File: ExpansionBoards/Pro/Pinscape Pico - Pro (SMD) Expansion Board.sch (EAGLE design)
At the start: 211 parts, among them IC1 UCC27523D, IC10 UCC27523D, IC11 UCC27523D, IC12 UCC27523D, IC13 UCC27523D, IC14 UCC27523D, IC15 TLC59116FIRHBR, IC16 TLC59116FIRHBR, IC17 TLC59116FIRHBR, IC18 TLC59116FIRHBR, IC19 ULN2803ADWR, IC2 UCC27523D, IC20 ULN2803ADWR, IC21 ULN2803ADWR, IC22 ULN2803ADWR, IC23 ULN2803ADWR, IC24 SN74HC165PWR, IC25 SN74HC165PWR, IC26 SN74HC165PWR, IC27 SN74HC165PWR, IC28 LIS3DHTR, IC29 SN74LVC1G175DCKR, IC3 UCC27523D, IC30 APX809S-29SA-7, IC31 LTV-827S, IC32 ADS1115IDGSR, IC33 TLV75733PDBVR, IC34 RV-3032-C7, IC4 UCC27523D, IC5 UCC27523D, IC6 UCC27523D, IC7 UCC27523D, IC8 UCC27523D, IC9 UCC27523D, J1 640445-6, J10 1-640456-0, J11 1-640456-0, J12 1-640456-0, J13 640445-5, J14 640445-9, J15 640445-9, J16 640445-9, J18 BM03B-SRSS-TB(LF)(SN), J2 30316-6002HB, J3 1-640456-0, J4 640456-9, J5 640456-9, J6 640454-2, J7 215079-4, J8 30308-6002HB, J9 1-640456-0, Q1 BUK7K89-100EX, Q10 BUK7K89-100EX, Q11 BUK7K89-100EX, Q12 BUK7K89-100EX, Q13 BUK7K89-100EX, Q14 BUK7K89-100EX, Q15 UMA5NTR, Q16 UMA5NTR, Q17 UMA5NTR, Q18 UMA5NTR, Q19 UMA5NTR, Q2 BUK7K89-100EX, Q20 UMA5NTR, Q21 UMA5NTR, Q22 UMA5NTR, Q23 UMA5NTR, Q24 UMA5NTR, Q25 UMA5NTR, Q26 UMA5NTR, Q29 DMG2302UK-7, Q3 BUK7K89-100EX, Q4 BUK7K89-100EX, Q5 BUK7K89-100EX, Q6 BUK7K89-100EX, Q7 BUK7K89-100EX, Q8 BUK7K89-100EX, Q9 BUK7K89-100EX, SW1 TS-1187A-B-A-B, U1 BAT-HLD-001-THM

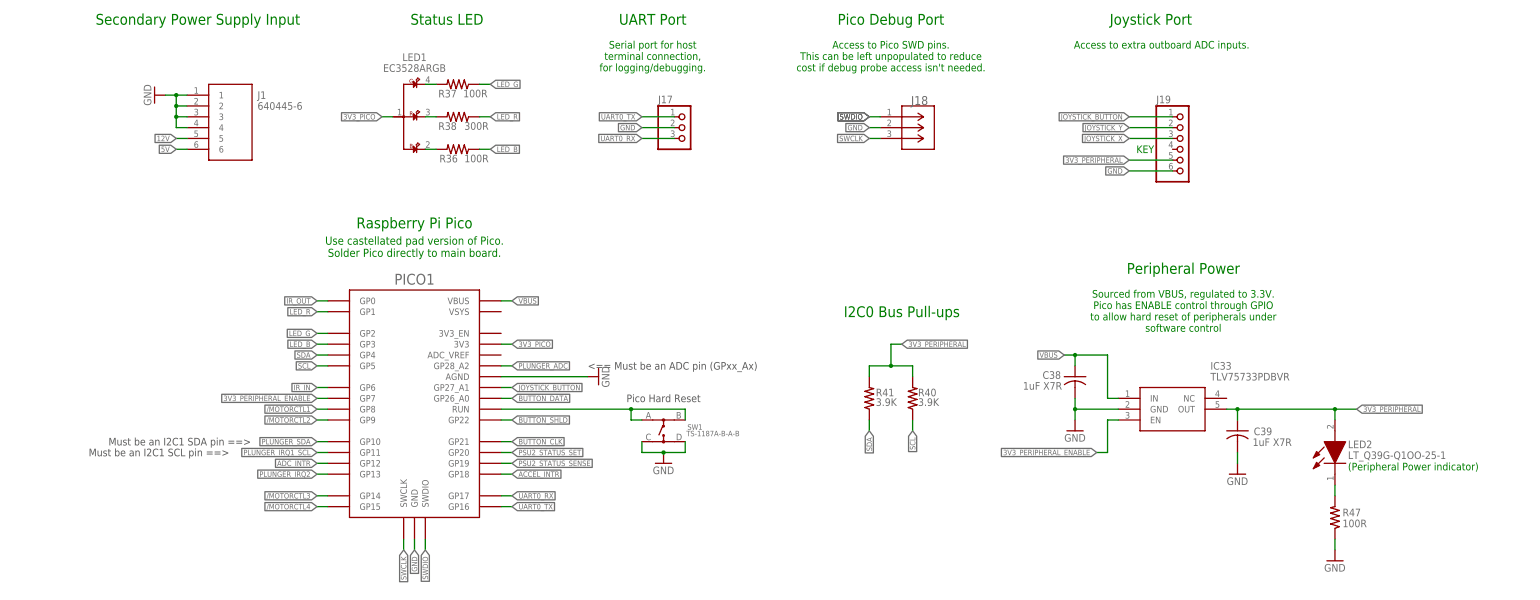
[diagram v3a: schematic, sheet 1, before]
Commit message: change to socketed Pico for Pro board
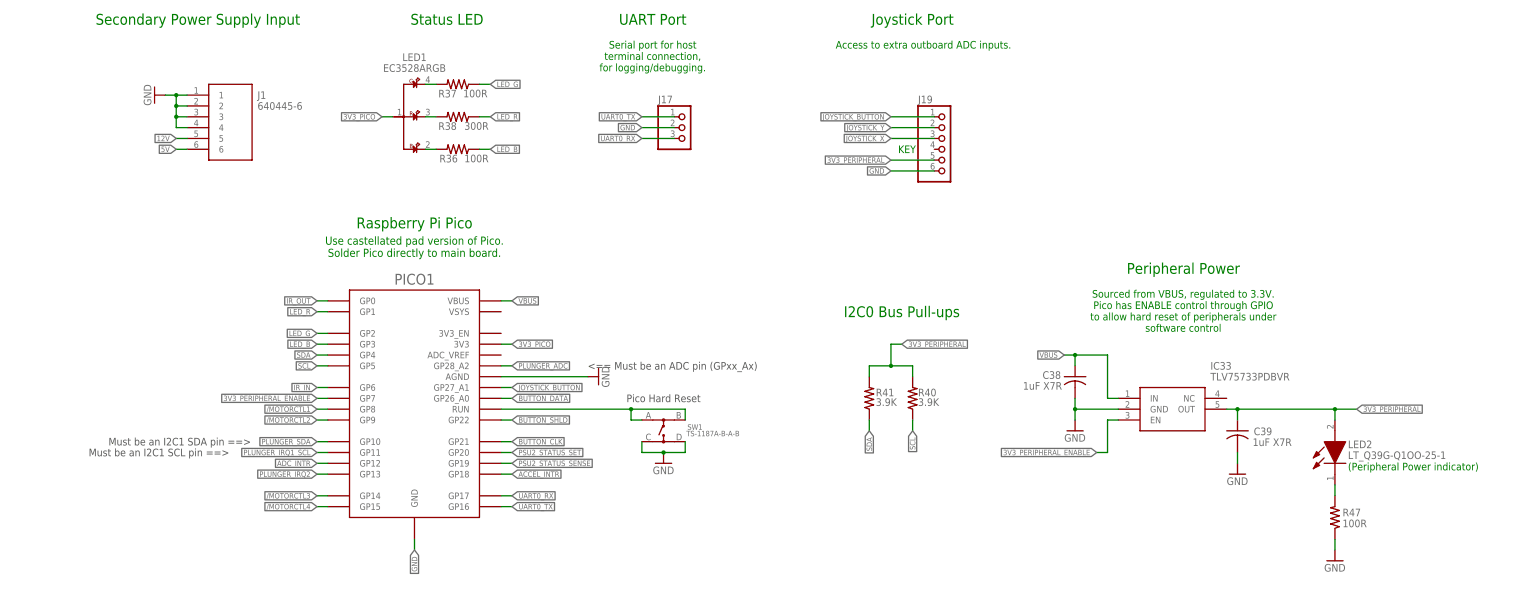
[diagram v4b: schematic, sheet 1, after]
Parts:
- removed J18: BM03B-SRSS-TB(LF)(SN), SamacSys_Parts:BM03B-SRSS-TB(LF)(SN)
- PICO1: device RaspberryPi_Pico:RPI_PICO-SMD -> RaspberryPi_Pico:RPI_PICO_NO_DEBUG
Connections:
- removed net SWCLK: J18.3, PICO1.SWCLK
- removed net SWDIO: J18.1, PICO1.SWDIO
- net GND: no longer J18.2
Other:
- note removed: "Access to Pico SWD pins. This can be left unpopulated to reduce cost if debug probe access isn't needed."
- note removed: "Pico Debug Port"
- moved on the sheet: J19

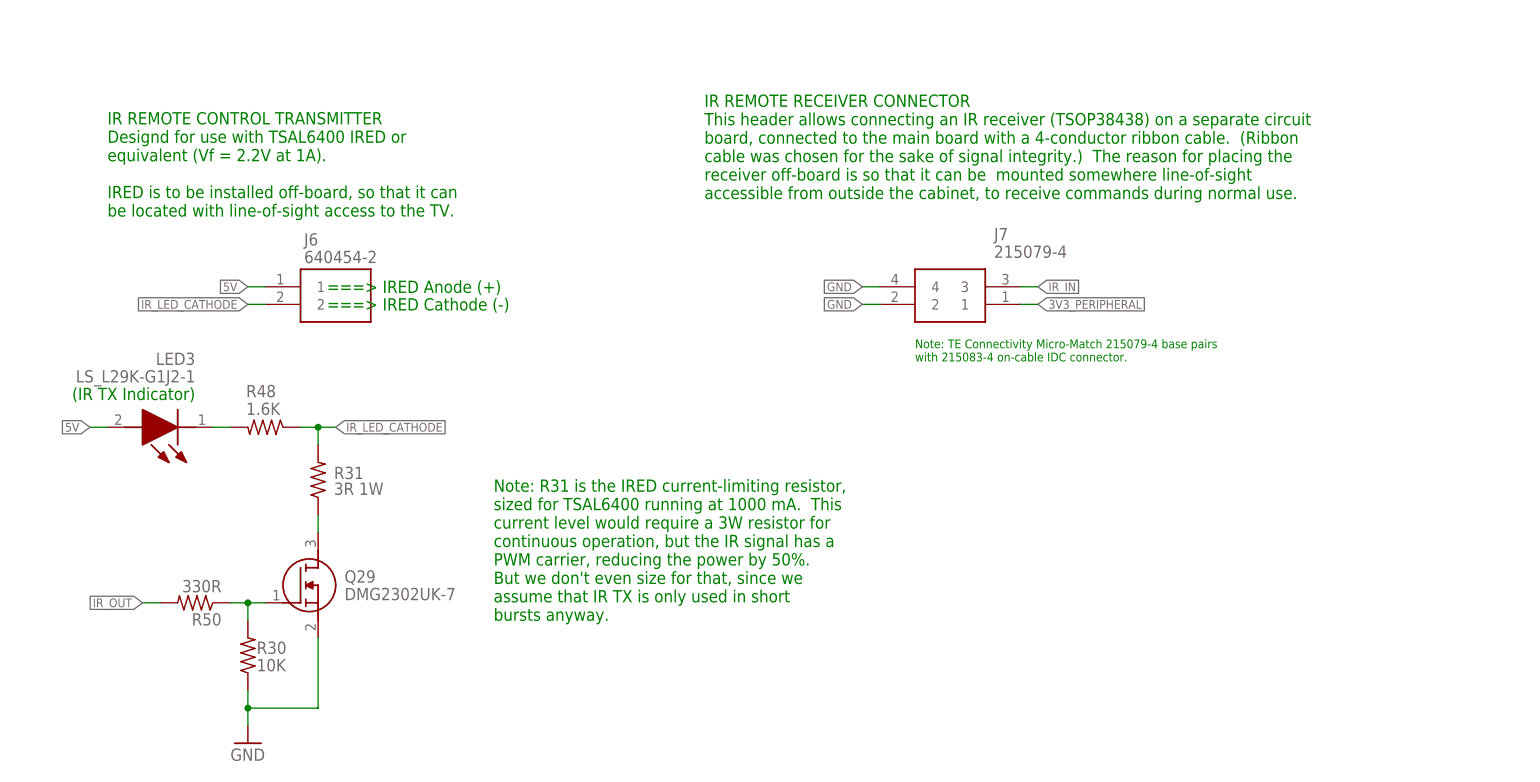
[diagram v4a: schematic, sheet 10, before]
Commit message: add tlc59116 wiring diagram to json doc; change Pro board IRED to constant-current circuit
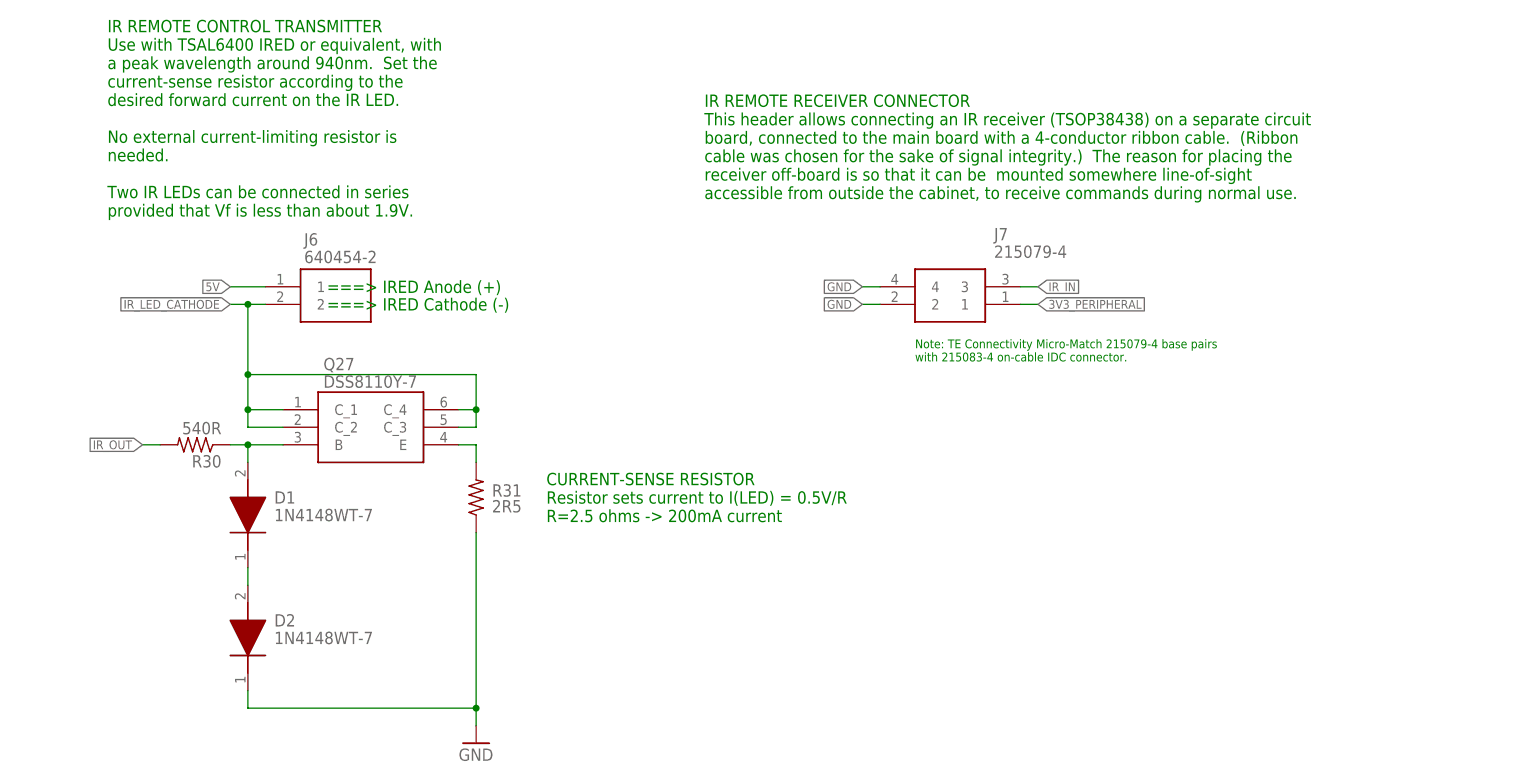
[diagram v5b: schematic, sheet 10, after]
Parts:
- removed LED3: LS_L29K-G1J2-1, SamacSys_Parts:LS_L29K-G1J2-1
- removed Q29: DMG2302UK-7, SamacSys_Parts:DMG2302UK-7
- removed R48: 1.6K, resistor:R-US_R0402
- removed R50: 330R, resistor:R-US_R0402
- added D1, D2: 1N4148WT-7, SamacSys_Parts:1N4148WT-7
- added Q27: DSS8110Y-7, SamacSys_Parts:DSS8110Y-7
- R30: value 10K -> 540R
- R31: value 3R 1W -> 2R5; device rcl:R-US_R2512 -> rcl:R-US_R0603
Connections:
- removed net N$75: LED3.K, R48.2
- new net N$81: D1.K, D2.A
- net 5V: no longer LED3.A
- net GND: now also D2.K, R31.1; no longer Q29.S, R30.1
- net IR_LED_CATHODE: now also Q27.C_1, Q27.C_2, Q27.C_3, Q27.C_4; no longer R31.2, R48.1
- net IR_OUT: now also R30.2; no longer R50.2
- net N$32: now also Q27.E, R31.2; no longer Q29.D, R31.1
- net N$77: now also D1.A, Q27.B, R30.1; no longer Q29.G, R30.2, R50.1
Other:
- note added: "CURRENT-SENSE RESISTOR Resistor sets current to I(LED) = 0.5V/R R=2.5 ohms -> 200mA current"
- note added: "IR REMOTE CONTROL TRANSMITTER Use with TSAL6400 IRED or equivalent, with a peak wavelength around 940nm. Set the current-sense resistor according to the desired forward current on the IR LED. No external current-limiting resistor is needed. Two IR LEDs can be connected in series provided that Vf is less than about 1.9V."
- note removed: "(IR TX Indicator)"
- note removed: "IR REMOTE CONTROL TRANSMITTER Designd for use with TSAL6400 IRED or equivalent (Vf = 2.2V at 1A). IRED is to be installed off-board, so that it can be located with line-of-sight access to the TV."
- note removed: "Note: R31 is the IRED current-limiting resistor, sized for TSAL6400 running at 1000 mA. This current level would require a 3W resistor for continuous operation, but the IR signal has a PWM carrier, reducing the power by 50%. But we don't even size for that, since we assume that IR TX is only used in short bursts anyway."
- moved on the sheet: R30, R31

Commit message: Update Pro and KL25Z adapter boards to make LIS3DH footprint compatible with LIS3DSH
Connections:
- net GND: now also IC28.ADC1, IC28.ADC2, IC28.ADC3
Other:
- note added: "Accelerometer - LIS3DH I2C Address 0x18 (001 1000)"
- note added: "Also pin-compatible with LIS3DSH (address 0x1E, 001 1110)"
- note removed: "Accelerometer"
- moved on the sheet: C35, IC28

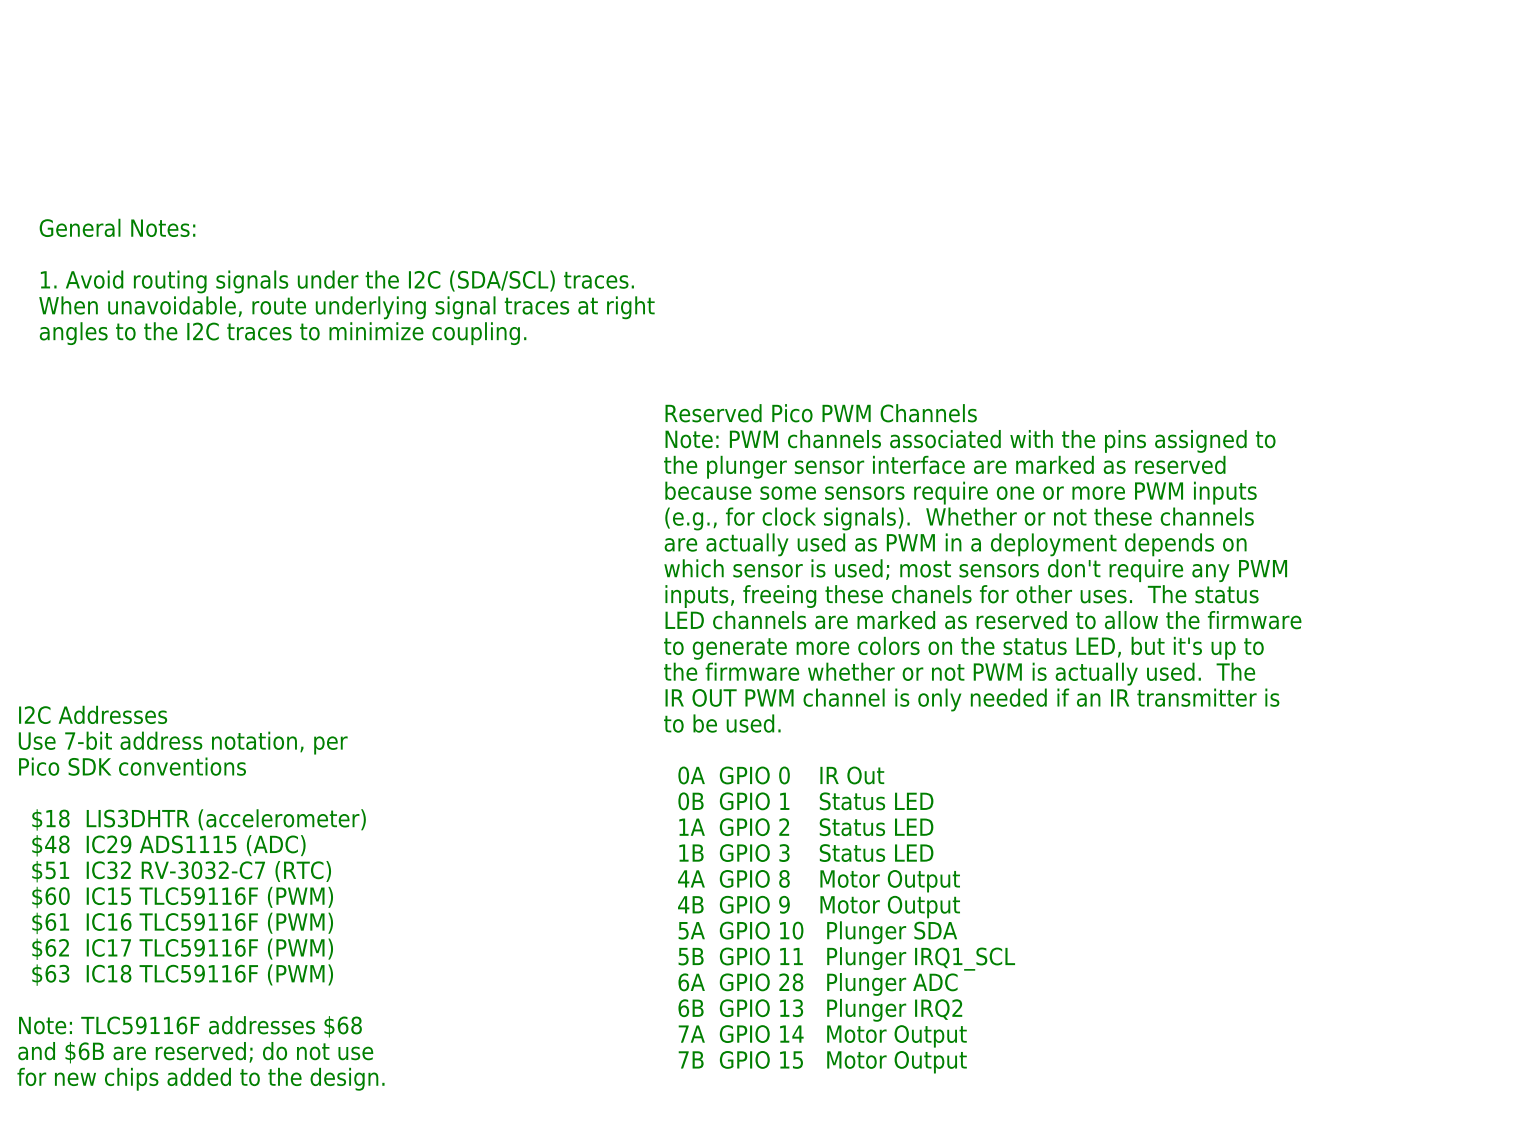
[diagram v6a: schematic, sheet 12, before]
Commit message: PCB parts lists (BOMs); power distro board edits
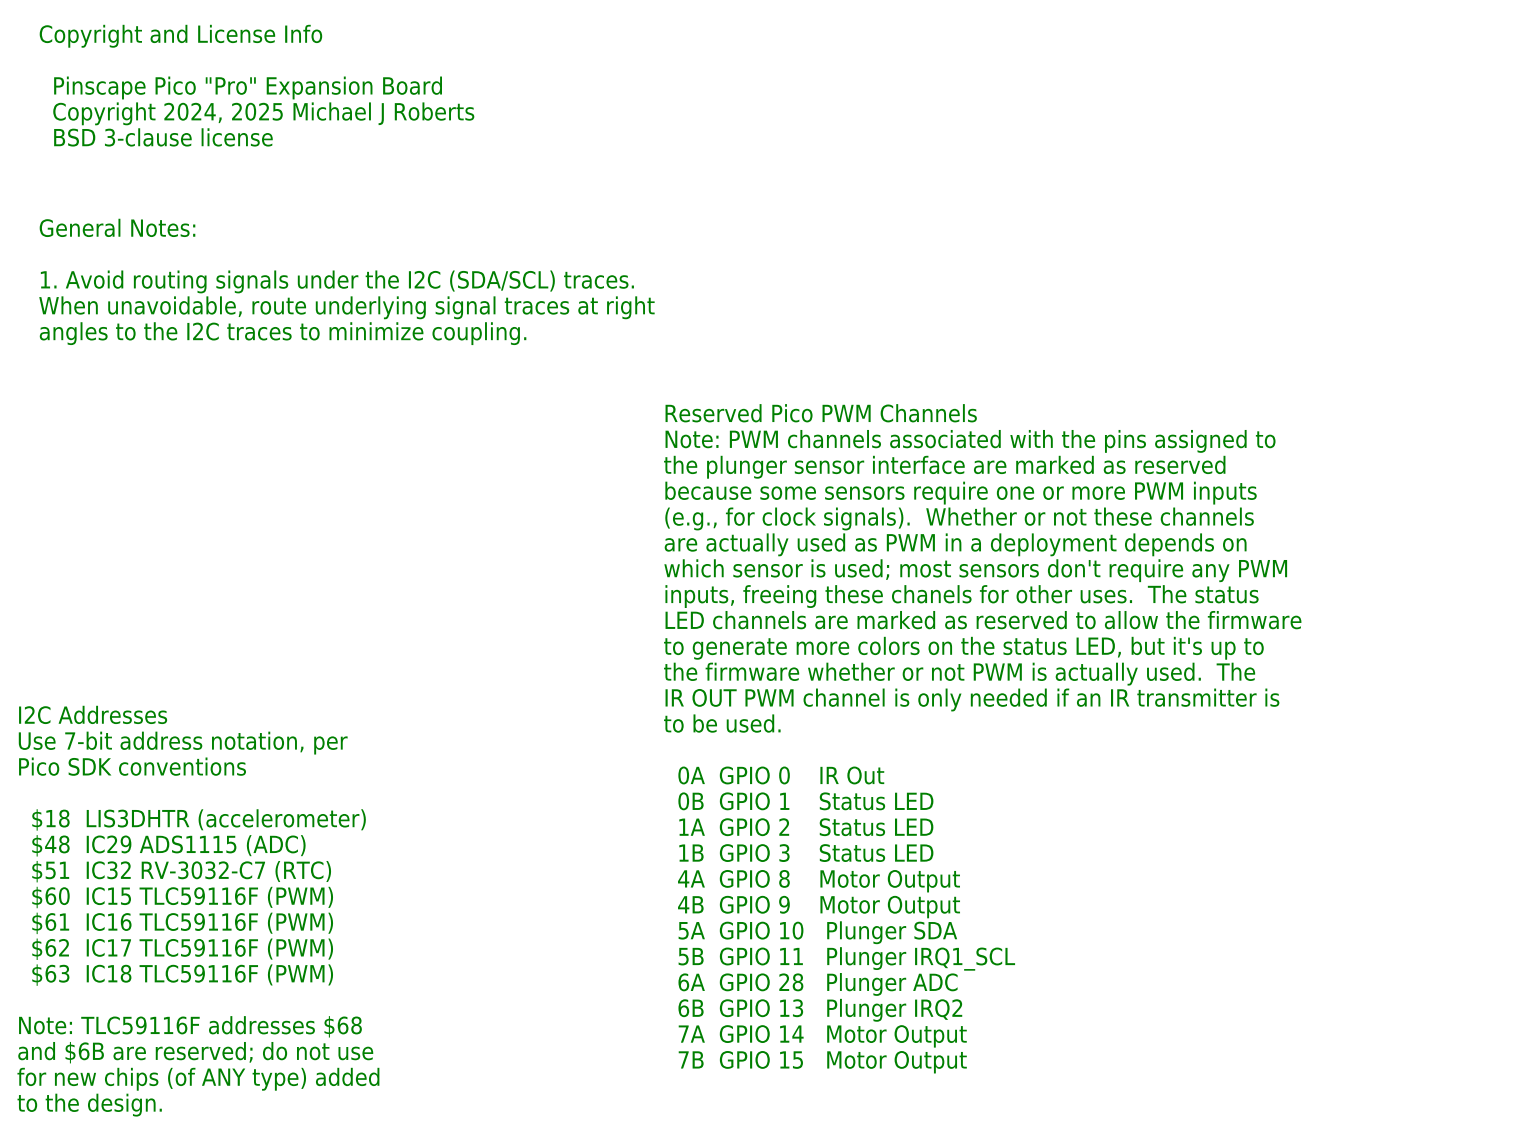
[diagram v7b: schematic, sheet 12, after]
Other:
- note added: "Copyright and License Info Pinscape Pico "Pro" Expansion Board Copyright 2024, 2025 Michael J Roberts BSD 3-clause license"
- note added: "I2C Addresses Use 7-bit address notation, per Pico SDK conventions $18 LIS3DHTR (accelerometer) $48 IC29 ADS1115 (ADC) $51 IC32 RV-3032-C7 (RTC) $60 IC15 TLC59116F (PWM) $61 IC16 TLC59116F (PWM) $62 IC17 TLC59116F (PWM) $63 IC18 TLC59116F (PWM) Note: TLC59116F addresses $68 and $6B are reserved; do not use for new chips (of ANY type) added to the design."
- note removed: "I2C Addresses Use 7-bit address notation, per Pico SDK conventions $18 LIS3DHTR (accelerometer) $48 IC29 ADS1115 (ADC) $51 IC32 RV-3032-C7 (RTC) $60 IC15 TLC59116F (PWM) $61 IC16 TLC59116F (PWM) $62 IC17 TLC59116F (PWM) $63 IC18 TLC59116F (PWM) Note: TLC59116F addresses $68 and $6B are reserved; do not use for new chips added to the design."
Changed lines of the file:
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@@
 Note: TLC59116F addresses $68
 and $6B are reserved; do not use
-for new chips added to the design.</text>
+for new chips (of ANY type) added
+to the design.</text>
 <text x="81.28" y="86.36" size="2.032" layer="91" align="top-left">Reserved Pico PWM Channels
 Note: PWM channels associated with the pins assigned to
@@
 When unavoidable, route underlying signal traces at right
 angles to the I2C traces to minimize coupling.</text>
+<text x="7.62" y="116.84" size="2.032" layer="91" ratio="12">Copyright and License Info
+  Pinscape Pico "Pro" Expansion Board
+  Copyright 2024, 2025 Michael J Roberts
+  BSD 3-clause license</text>
 </plain>
 <instances>
